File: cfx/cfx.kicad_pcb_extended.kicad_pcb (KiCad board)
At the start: 2 copper layers, 26 x 34.5 mm, 2 parts, among them J1 CFExpress_Media, J2 Conn_01x30_Female

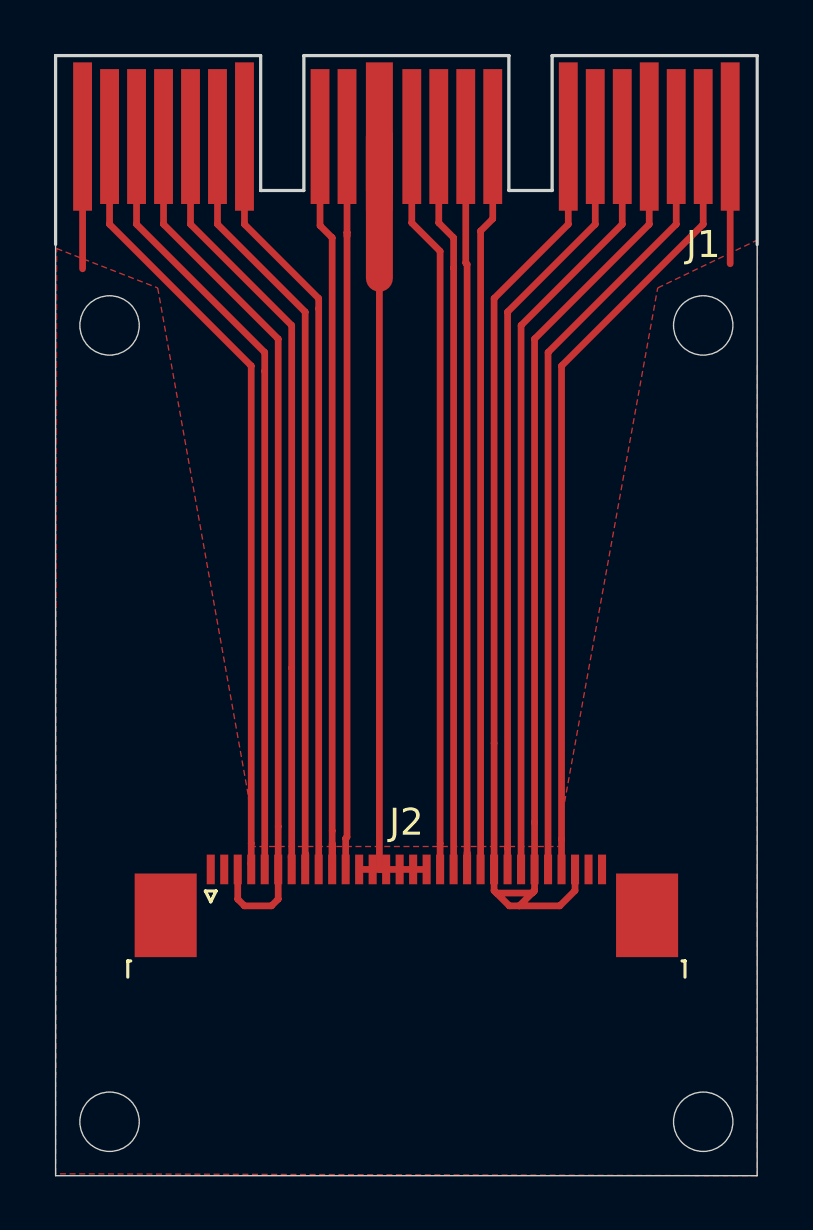
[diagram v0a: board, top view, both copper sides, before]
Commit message: Fixed path to tracks
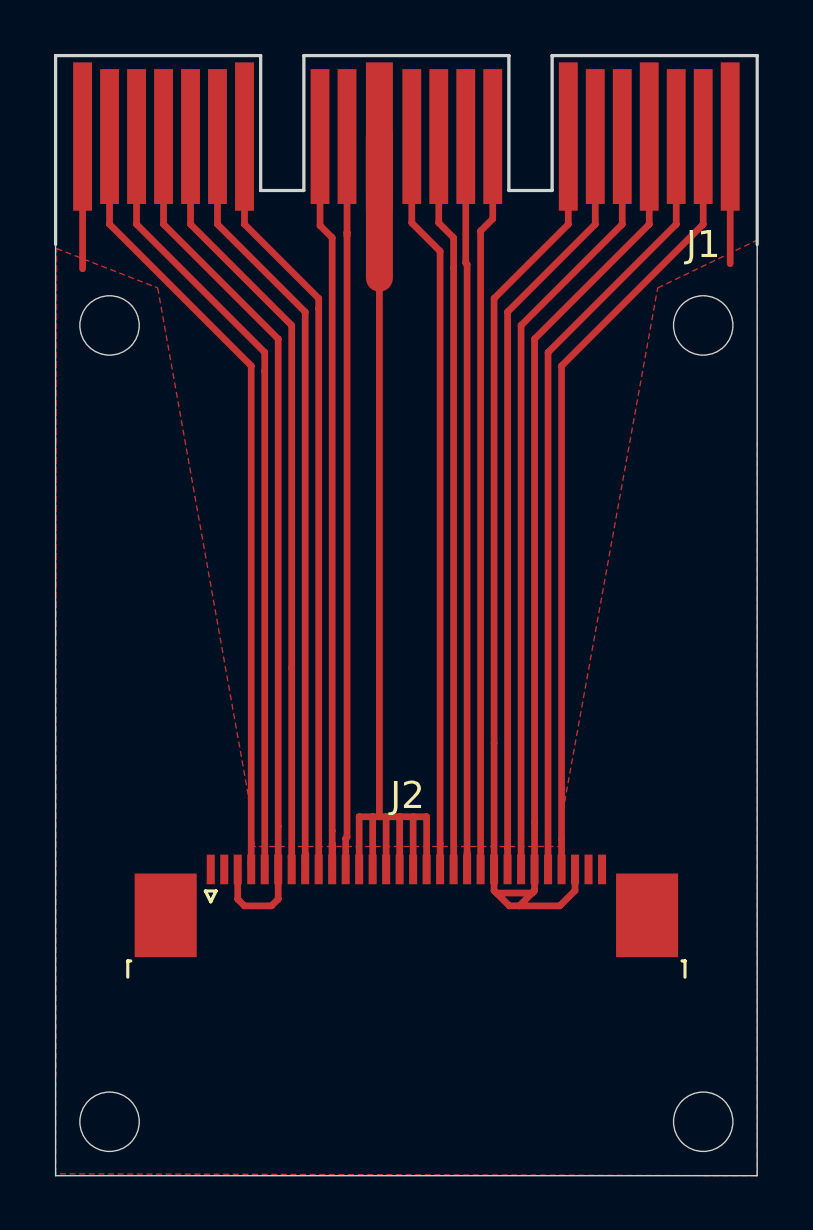
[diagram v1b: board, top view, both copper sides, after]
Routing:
- net +3V3: track 31.7 -> 41.4 mm
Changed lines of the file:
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@@
     (thickness 1.6)
     (drawings 8)
-    (tracks 100)
+    (tracks 115)
     (zones 0)
     (modules 2)
@@
       (effects (font (size 1 1) (thickness 0.15)))
     )
-    (fp_text value CFExpress_Media (at 13.23 11.69) (layer F.Fab)
+    (fp_text value CFExpress_Media (at 13.23 14.23) (layer F.Fab)
       (effects (font (size 1 1) (thickness 0.15)))
     )
@@
     (tags "te fpc 1734839")
     (attr smd)
-    (fp_text reference J2 (at 0 -3.1) (layer F.SilkS)
+    (fp_text reference J2 (at 0.0428 -4.0908) (layer F.SilkS)
       (effects (font (size 1 1) (thickness 0.15)))
     )
@@
   (segment (start 62 53) (end 62 55) (width 1) (layer F.Cu) (net 17))
   (segment (start 62 53) (end 62 58.25) (width 1) (layer F.Cu) (net 17))
-  (segment (start 62 80.1435) (end 62.0165 80.16) (width 0.25) (layer F.Cu) (net 17))
-  (segment (start 62 58.25) (end 62 80.1435) (width 0.25) (layer F.Cu) (net 17))
-  (segment (start 62.0165 80.16) (end 63.75 80.16) (width 0.25) (layer F.Cu) (net 17))
-  (segment (start 61.25 80.16) (end 62.0165 80.16) (width 0.25) (layer F.Cu) (net 17))
+  (segment (start 62 58.25) (end 62 78.208) (width 0.25) (layer F.Cu) (net 17))
+  (segment (start 63.75 78.2106) (end 63.75 80.16) (width 0.25) (layer F.Cu) (net 17))
+  (segment (start 63.7526 78.208) (end 63.75 78.2106) (width 0.25) (layer F.Cu) (net 17))
+  (segment (start 61.25 80.16) (end 61.25 78.20661) (width 0.25) (layer F.Cu) (net 17))
+  (segment (start 61.25 78.20661) (end 61.25139 78.208) (width 0.25) (layer F.Cu) (net 17))
+  (segment (start 61.75 78.2092) (end 61.7488 78.208) (width 0.25) (layer F.Cu) (net 17))
+  (segment (start 61.75 80.16) (end 61.75 78.2092) (width 0.25) (layer F.Cu) (net 17))
+  (segment (start 61.7488 78.208) (end 62 78.208) (width 0.25) (layer F.Cu) (net 17))
+  (segment (start 61.25139 78.208) (end 61.7488 78.208) (width 0.25) (layer F.Cu) (net 17))
+  (segment (start 62.25 78.212) (end 62.254 78.208) (width 0.25) (layer F.Cu) (net 17))
+  (segment (start 62.25 80.16) (end 62.25 78.212) (width 0.25) (layer F.Cu) (net 17))
+  (segment (start 62 78.208) (end 62.254 78.208) (width 0.25) (layer F.Cu) (net 17))
+  (segment (start 62.75 78.22) (end 62.762 78.208) (width 0.25) (layer F.Cu) (net 17))
+  (segment (start 62.75 80.16) (end 62.75 78.22) (width 0.25) (layer F.Cu) (net 17))
+  (segment (start 62.254 78.208) (end 62.762 78.208) (width 0.25) (layer F.Cu) (net 17))
+  (segment (start 63.25 78.228) (end 63.27 78.208) (width 0.25) (layer F.Cu) (net 17))
+  (segment (start 63.27 78.208) (end 63.7526 78.208) (width 0.25) (layer F.Cu) (net 17))
+  (segment (start 63.25 80.16) (end 63.25 78.228) (width 0.25) (layer F.Cu) (net 17))
+  (segment (start 62.762 78.208) (end 63.27 78.208) (width 0.25) (layer F.Cu) (net 17))
   (zone (net 16) (net_name GND) (layer F.Cu) (hatch edge 0.508)
     (connect_pads yes (clearance 0.254))
